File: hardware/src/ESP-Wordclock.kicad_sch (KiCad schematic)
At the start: 0 parts

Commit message: Add: Topology of the schematics
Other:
- added sheet Brightness Sensor (BrightnessSensor.kicad_sch)
- added sheet LEDs (LEDs.kicad_sch)
- added sheet MCU (MCU.kicad_sch)
- added sheet RTC (RTC.kicad_sch)
- added sheet USB (USB.kicad_sch)
- title: <Default Template> -> Wordclock - Top
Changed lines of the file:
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@@
 	(paper "A4")
 	(title_block
-		(title "<Default Template>")
-		(date "2023-04-28")
+		(title "Wordclock - Top")
+		(date "2024-10-19")
 		(rev "A")
 		(company "ElektroNik Zoller")
@@
 		(comment 4 "CERN-OHL-P")
 	)
+	(sheet
+		(at 62.23 36.83)
+		(size 26.67 29.21)
+		(fields_autoplaced yes)
+		(stroke
+			(width 0.1524)
+			(type solid)
+		)
+		(fill
+			(color 0 0 0 0.0000)
+		)
+		(property "Sheetname" "MCU"
+			(at 62.23 36.1184 0)
+			(effects
+				(font
+					(size 1.27 1.27)
+				)
+				(justify left bottom)
+			)
+		)
+		(property "Sheetfile" "MCU.kicad_sch"
+			(at 62.23 66.6246 0)
+			(effects
+				(font
+					(size 1.27 1.27)
+				)
+				(justify left top)
+			)
+		)
+		(instances
+			(project "ESP-Wordclock"
+				(path "/bfaac094-0365-40a4-8b7a-d4d62ace544e"
+					(page "10")
+				)
+			)
+		)
+	)
+	(sheet
+		(at 25.4 39.37)
+		(size 12.7 29.21)
+		(fields_autoplaced yes)
+		(stroke
+			(width 0.1524)
+			(type solid)
+		)
+		(fill
+			(color 0 0 0 0.0000)
+		)
+		(property "Sheetname" "USB"
+			(at 25.4 38.6584 0)
+			(effects
+				(font
+					(size 1.27 1.27)
+				)
+				(justify left bottom)
+			)
+		)
+		(property "Sheetfile" "USB.kicad_sch"
+			(at 25.4 69.1646 0)
+			(effects
+				(font
+					(size 1.27 1.27)
+				)
+				(justify left top)
+			)
+		)
+		(instances
+			(project "ESP-Wordclock"
+				(path "/bfaac094-0365-40a4-8b7a-d4d62ace544e"
+					(page "20")
+				)
+			)
+		)
+	)
+	(sheet
+		(at 163.83 115.57)
+		(size 39.37 20.32)
+		(fields_autoplaced yes)
+		(stroke
+			(width 0.1524)
+			(type solid)
+		)
+		(fill
+			(color 0 0 0 0.0000)
+		)
+		(property "Sheetname" "LEDs"
+			(at 163.83 114.8584 0)
+			(effects
+				(font
+					(size 1.27 1.27)
+				)
+				(justify left bottom)
+			)
+		)
+		(property "Sheetfile" "LEDs.kicad_sch"
+			(at 163.83 136.4746 0)
+			(effects
+				(font
+					(size 1.27 1.27)
+				)
+				(justify left top)
+			)
+		)
+		(instances
+			(project "ESP-Wordclock"
+				(path "/bfaac094-0365-40a4-8b7a-d4d62ace544e"
+					(page "50")
+				)
+			)
+		)
+	)
+	(sheet
+		(at 113.03 39.37)
+		(size 26.67 26.67)
+		(fields_autoplaced yes)
+		(stroke
+			(width 0.1524)
+			(type solid)
+		)
+		(fill
+			(color 0 0 0 0.0000)
+		)
+		(property "Sheetname" "RTC"
+			(at 113.03 38.6584 0)
+			(effects
+				(font
+					(size 1.27 1.27)
+				)
+				(justify left bottom)
+			)
+		)
+		(property "Sheetfile" "RTC.kicad_sch"
+			(at 113.03 66.6246 0)
+			(effects
+				(font
+					(size 1.27 1.27)
+				)
+				(justify left top)
+			)
+		)
+		(instances
+			(project "ESP-Wordclock"
+				(path "/bfaac094-0365-40a4-8b7a-d4d62ace544e"
+					(page "30")
+				)
+			)
+		)
+	)
+	(sheet
+		(at 163.83 39.37)
+		(size 33.02 34.29)
+		(fields_autoplaced yes)
+		(stroke
+			(width 0.1524)
+			(type solid)
+		)
+		(fill
+			(color 0 0 0 0.0000)
+		)
+		(property "Sheetname" "Brightness Sensor"
+			(at 163.83 38.6584 0)
+			(effects
+				(font
+					(size 1.27 1.27)
+				)
+				(justify left bottom)
+			)
+		)
+		(property "Sheetfile" "BrightnessSensor.kicad_sch"
+			(at 163.83 74.2446 0)
+			(effects
+				(font
+					(size 1.27 1.27)
+				)
+				(justify left top)
+			)
+		)
+		(instances
+			(project "ESP-Wordclock"
+				(path "/bfaac094-0365-40a4-8b7a-d4d62ace544e"
+					(page "40")
+				)
+			)
+		)
+	)
 	(sheet_instances

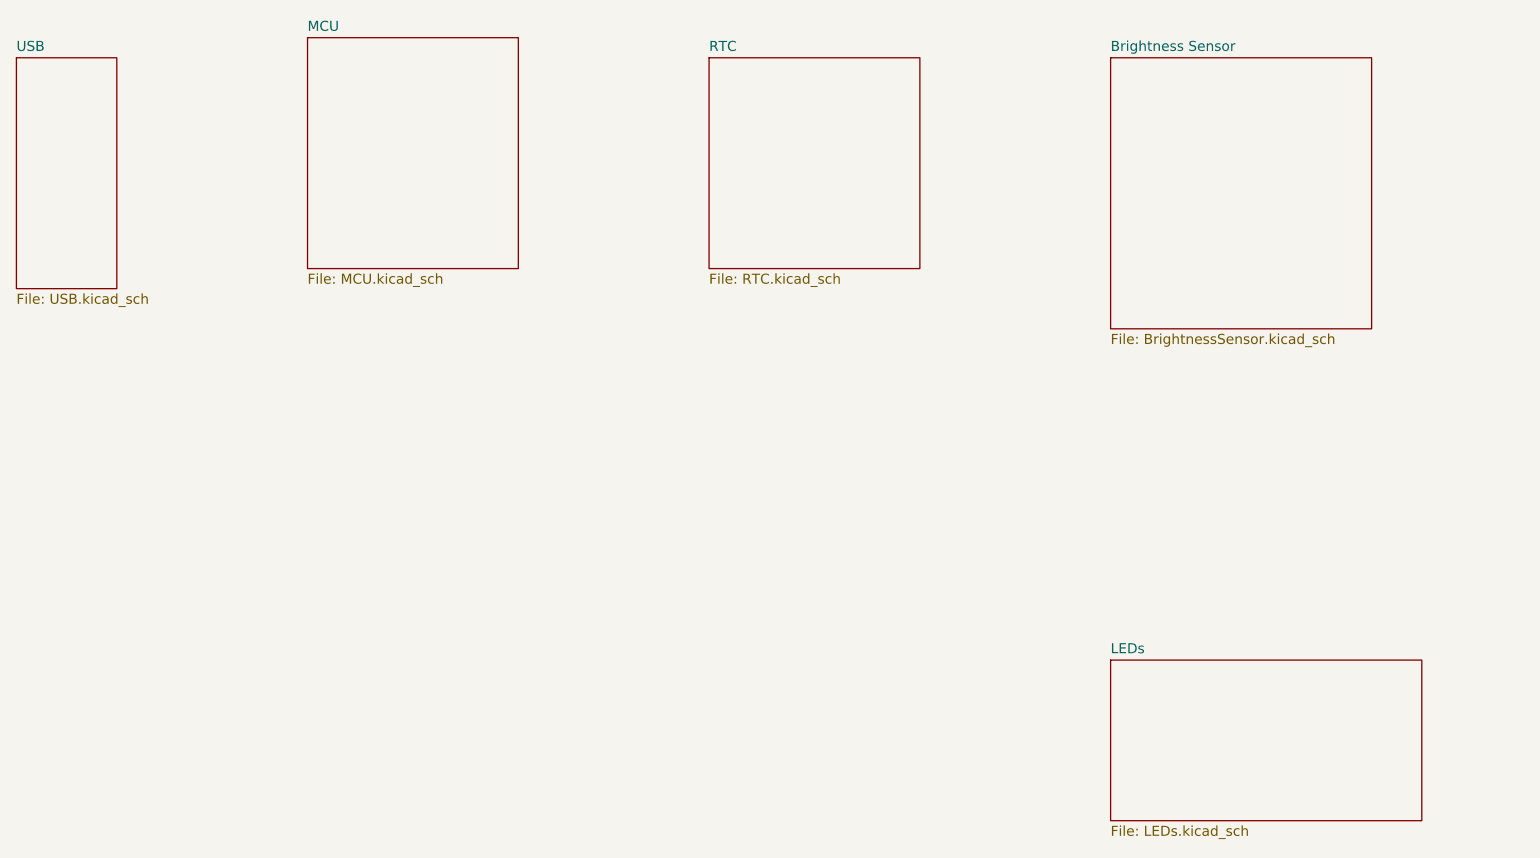
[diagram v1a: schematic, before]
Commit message: Add: MCU and power supply. And connected to USB in top level schematic
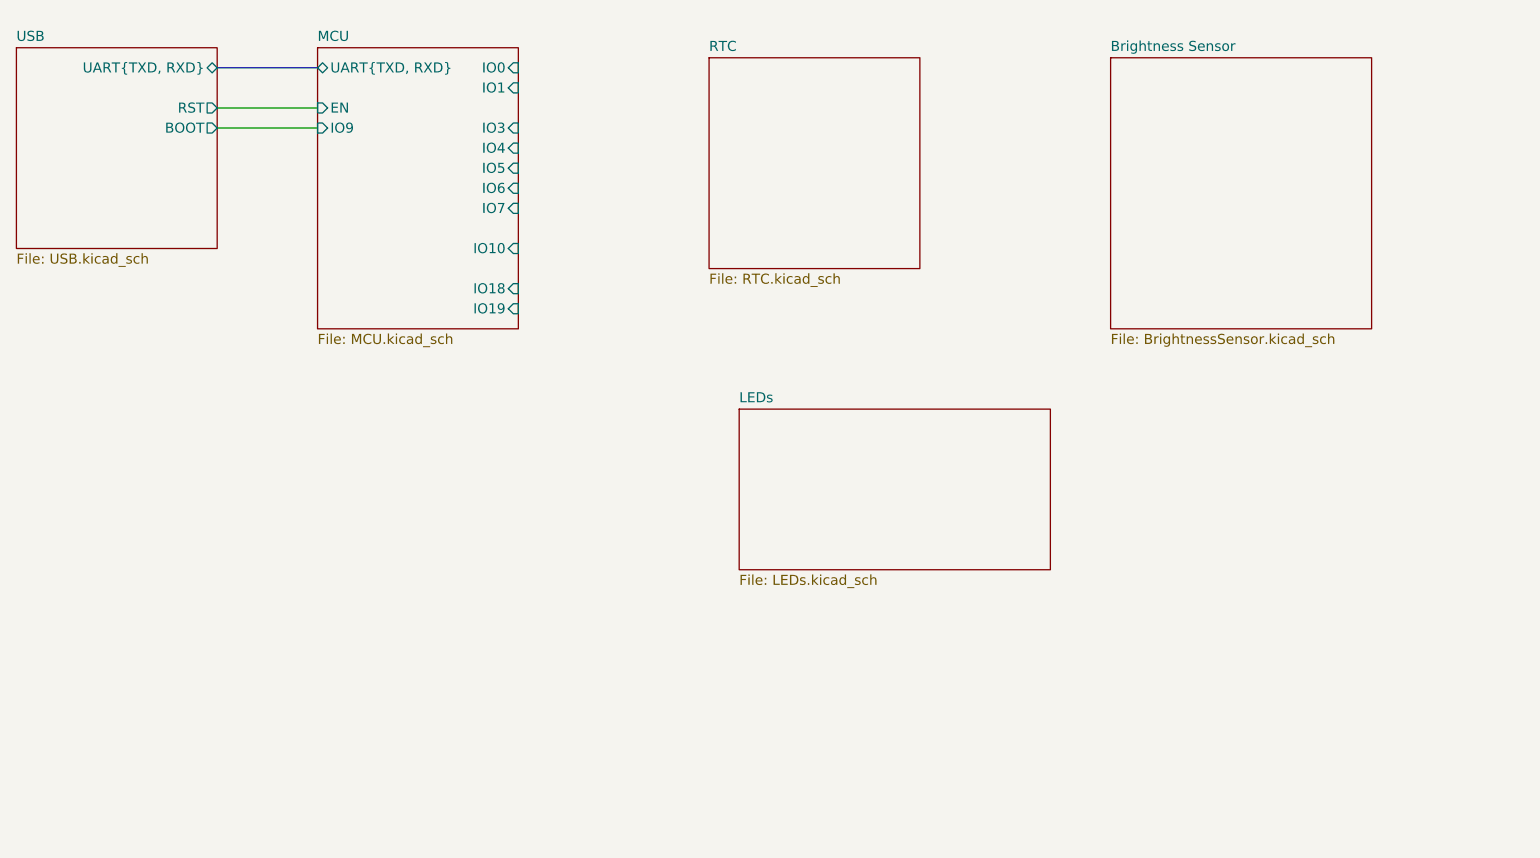
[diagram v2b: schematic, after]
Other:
- sheet MCU ports: added EN, IO0, IO1, IO10, IO18, IO19, IO3, IO4, IO5, IO6, IO7, IO9, UART{TXD, RXD}; removed none
- sheet USB ports: added BOOT, RST, UART{TXD, RXD}; removed none
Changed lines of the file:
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@@
 		(comment 4 "CERN-OHL-P")
 	)
+	(wire
+		(pts
+			(xy 50.8 48.26) (xy 63.5 48.26)
+		)
+		(stroke
+			(width 0)
+			(type default)
+		)
+	)
+	(wire
+		(pts
+			(xy 50.8 45.72) (xy 63.5 45.72)
+		)
+		(stroke
+			(width 0)
+			(type default)
+		)
+	)
+	(bus
+		(pts
+			(xy 50.8 40.64) (xy 63.5 40.64)
+		)
+		(stroke
+			(width 0)
+			(type default)
+		)
+	)
 	(sheet
-		(at 62.23 36.83)
-		(size 26.67 29.21)
+		(at 63.5 38.1)
+		(size 25.4 35.56)
 		(fields_autoplaced yes)
 		(stroke
@@
 		)
 		(property "Sheetname" "MCU"
-			(at 62.23 36.1184 0)
+			(at 63.5 37.3884 0)
 			(effects
 				(font
@@
 		)
 		(property "Sheetfile" "MCU.kicad_sch"
-			(at 62.23 66.6246 0)
+			(at 63.5 74.2446 0)
 			(effects
 				(font
@@
 				)
 				(justify left top)
+			)
+		)
+		(pin "IO10" input
+			(at 88.9 63.5 0)
+			(effects
+				(font
+					(size 1.27 1.27)
+				)
+				(justify right)
+			)
+		)
+		(pin "IO18" input
+			(at 88.9 68.58 0)
+			(effects
+				(font
+					(size 1.27 1.27)
+				)
+				(justify right)
+			)
+		)
+		(pin "IO9" input
+			(at 63.5 48.26 180)
+			(effects
+				(font
+					(size 1.27 1.27)
+				)
+				(justify left)
+			)
+		)
+		(pin "IO19" input
+			(at 88.9 71.12 0)
+			(effects
+				(font
+					(size 1.27 1.27)
+				)
+				(justify right)
+			)
+		)
+		(pin "IO4" input
+			(at 88.9 50.8 0)
+			(effects
+				(font
+					(size 1.27 1.27)
+				)
+				(justify right)
+			)
+		)
+		(pin "IO3" input
+			(at 88.9 48.26 0)
+			(effects
+				(font
+					(size 1.27 1.27)
+				)
+				(justify right)
+			)
+		)
+		(pin "IO5" input
+			(at 88.9 53.34 0)
+			(effects
+				(font
+					(size 1.27 1.27)
+				)
+				(justify right)
+			)
+		)
+		(pin "IO6" input
+			(at 88.9 55.88 0)
+			(effects
+				(font
+					(size 1.27 1.27)
+				)
+				(justify right)
+			)
+		)
+		(pin "IO7" input
+			(at 88.9 58.42 0)
+			(effects
+				(font
+					(size 1.27 1.27)
+				)
+				(justify right)
+			)
+		)
+		(pin "UART{TXD, RXD}" bidirectional
+			(at 63.5 40.64 180)
+			(effects
+				(font
+					(size 1.27 1.27)
+				)
+				(justify left)
+			)
+		)
+		(pin "EN" input
+			(at 63.5 45.72 180)
+			(effects
+				(font
+					(size 1.27 1.27)
+				)
+				(justify left)
+			)
+		)
+		(pin "IO1" input
+			(at 88.9 43.18 0)
+			(effects
+				(font
+					(size 1.27 1.27)
+				)
+				(justify right)
+			)
+		)
+		(pin "IO0" input
+			(at 88.9 40.64 0)
+			(effects
+				(font
+					(size 1.27 1.27)
+				)
+				(justify right)
 			)
 		)
@@
 	)
 	(sheet
-		(at 25.4 39.37)
-		(size 12.7 29.21)
+		(at 25.4 38.1)
+		(size 25.4 25.4)
 		(fields_autoplaced yes)
 		(stroke
@@
 		)
 		(property "Sheetname" "USB"
-			(at 25.4 38.6584 0)
+			(at 25.4 37.3884 0)
 			(effects
 				(font
@@
 		)
 		(property "Sheetfile" "USB.kicad_sch"
-			(at 25.4 69.1646 0)
+			(at 25.4 64.0846 0)
 			(effects
 				(font
@@
 				)
 				(justify left top)
+			)
+		)
+		(pin "UART{TXD, RXD}" bidirectional
+			(at 50.8 40.64 0)
+			(effects
+				(font
+					(size 1.27 1.27)
+				)
+				(justify right)
+			)
+		)
+		(pin "BOOT" output
+			(at 50.8 48.26 0)
+			(effects
+				(font
+					(size 1.27 1.27)
+				)
+				(justify right)
+			)
+		)
+		(pin "RST" output
+			(at 50.8 45.72 0)
+			(effects
+				(font
+					(size 1.27 1.27)
+				)
+				(justify right)
 			)
 		)
@@
 	)
 	(sheet
-		(at 163.83 115.57)
+		(at 116.84 83.82)
 		(size 39.37 20.32)
 		(fields_autoplaced yes)
@@
 		)
 		(property "Sheetname" "LEDs"
-			(at 163.83 114.8584 0)
+			(at 116.84 83.1084 0)
 			(effects
 				(font
@@
 		)
 		(property "Sheetfile" "LEDs.kicad_sch"
-			(at 163.83 136.4746 0)
-			(effects
-				(font
+			(at 116.84 104.7246 0)
+			(effects
+				(font

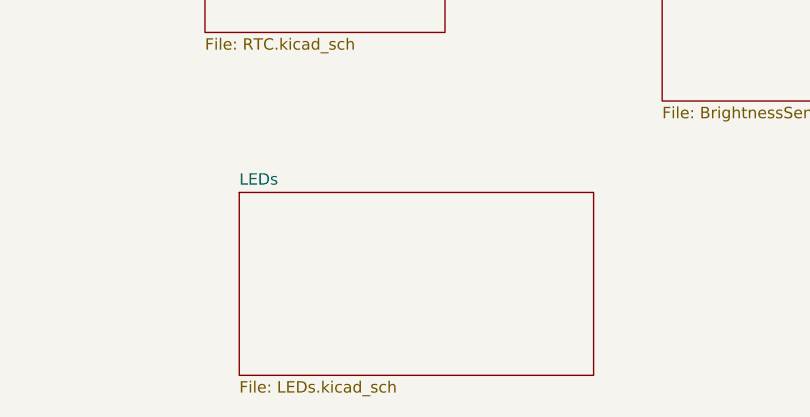
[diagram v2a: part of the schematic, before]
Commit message: Add: LEDs to the schematic
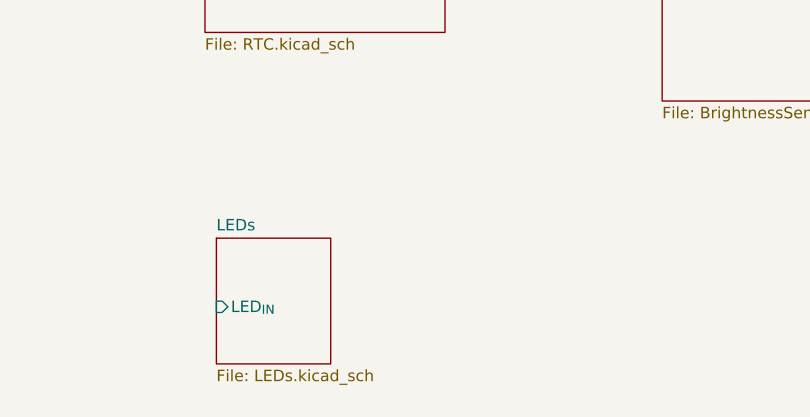
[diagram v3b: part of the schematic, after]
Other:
- sheet LEDs ports: added LED_{IN}; removed none
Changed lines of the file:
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@@
 			(project "ESP-Wordclock"
 				(path "/bfaac094-0365-40a4-8b7a-d4d62ace544e"
-					(page "10")
+					(page "2")
 				)
 			)
@@
 			(project "ESP-Wordclock"
 				(path "/bfaac094-0365-40a4-8b7a-d4d62ace544e"
-					(page "20")
+					(page "3")
 				)
 			)
@@
 	)
 	(sheet
-		(at 116.84 83.82)
-		(size 39.37 20.32)
+		(at 114.3 88.9)
+		(size 12.7 13.97)
 		(fields_autoplaced yes)
 		(stroke
@@
 		)
 		(property "Sheetname" "LEDs"
-			(at 116.84 83.1084 0)
+			(at 114.3 88.1884 0)
 			(effects
 				(font
@@
 		)
 		(property "Sheetfile" "LEDs.kicad_sch"
-			(at 116.84 104.7246 0)
+			(at 114.3 103.4546 0)
 			(effects
 				(font
@@
 			)
 		)
+		(pin "LED_{IN}" input
+			(at 114.3 96.52 180)
+			(effects
+				(font
+					(size 1.27 1.27)
+				)
+				(justify left)
+			)
+		)
 		(instances
 			(project "ESP-Wordclock"
 				(path "/bfaac094-0365-40a4-8b7a-d4d62ace544e"
-					(page "50")
+					(page "6")
 				)
 			)
@@
 			(project "ESP-Wordclock"
 				(path "/bfaac094-0365-40a4-8b7a-d4d62ace544e"
-					(page "30")
+					(page "4")
 				)
 			)
@@
 			(project "ESP-Wordclock"
 				(path "/bfaac094-0365-40a4-8b7a-d4d62ace544e"
-					(page "40")
+					(page "5")
 				)
 			)

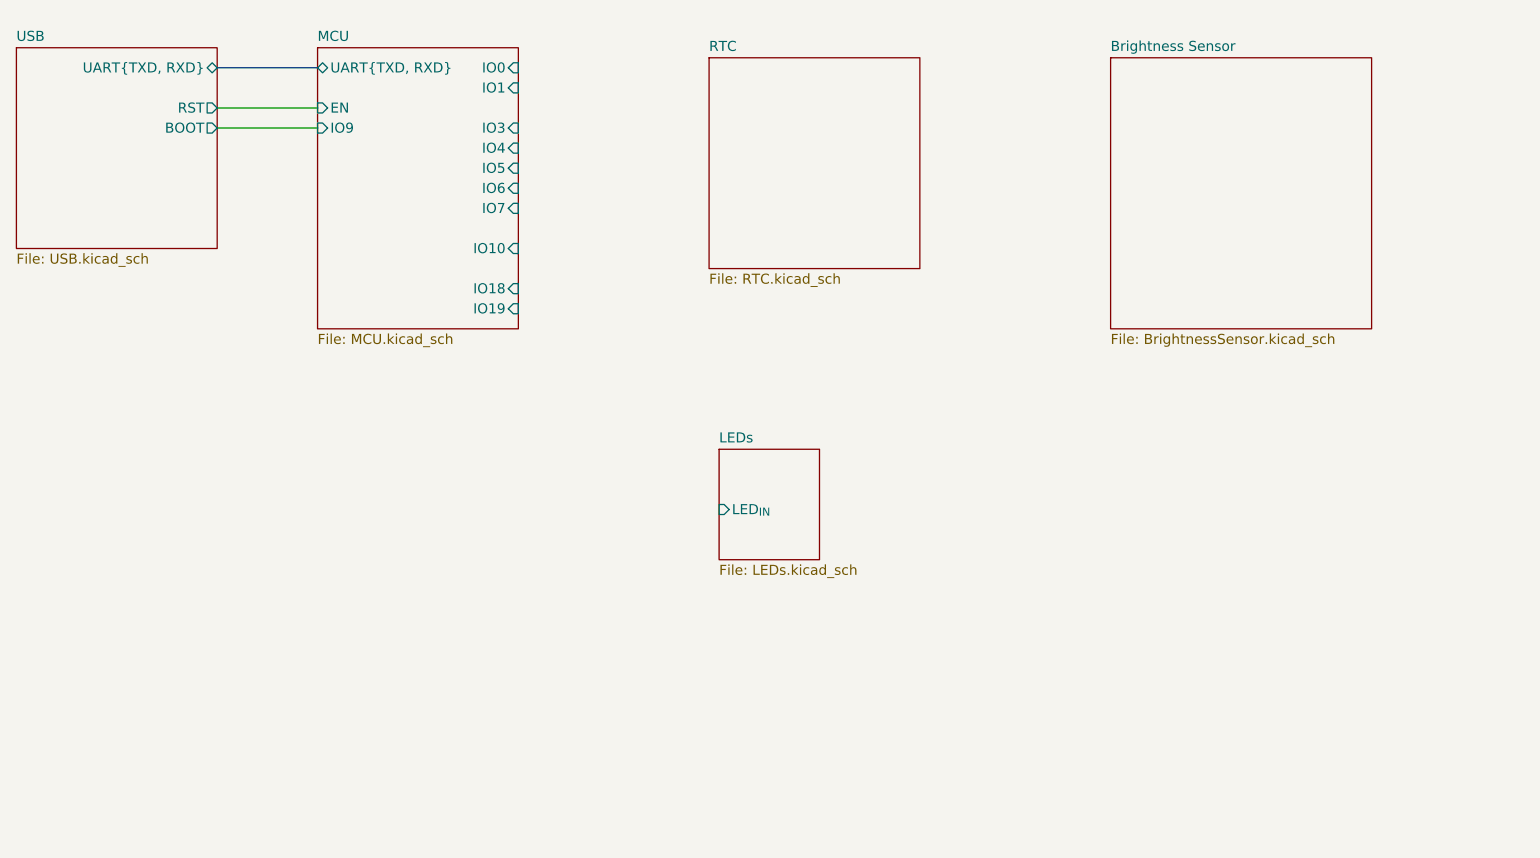
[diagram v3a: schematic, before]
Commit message: Add: RTC schematic
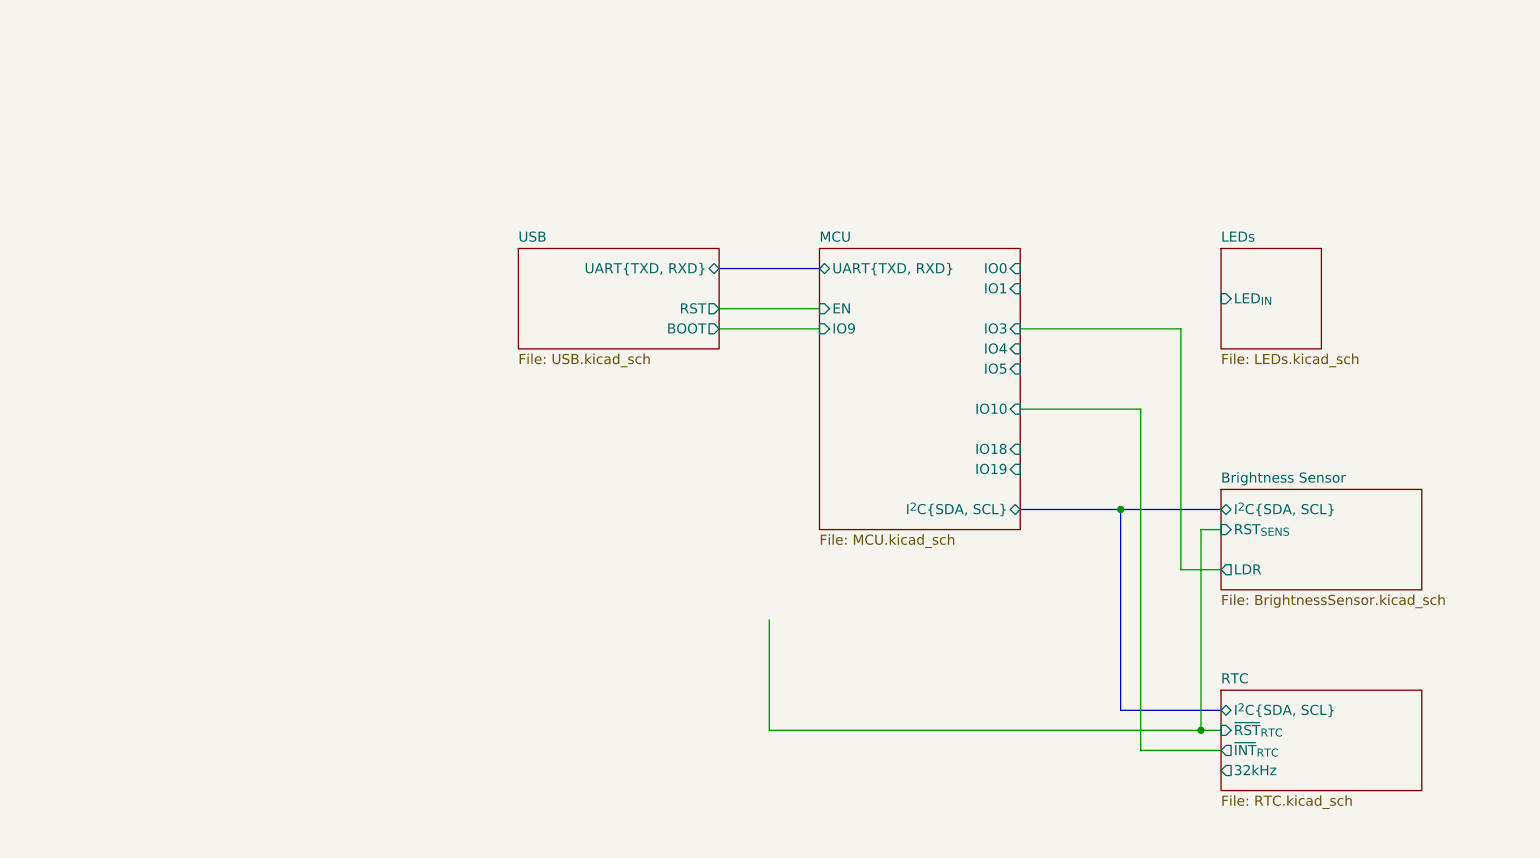
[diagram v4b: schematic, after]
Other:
- sheet Brightness Sensor ports: added I^{2}C{SDA, SCL}, LDR, RST_{SENS}; removed none
- sheet MCU ports: added I^{2}C{SDA, SCL}; removed IO6, IO7
- sheet RTC ports: added 32kHz, I^{2}C{SDA, SCL}, ~{INT}_{RTC}, ~{RST}_{RTC}; removed none
